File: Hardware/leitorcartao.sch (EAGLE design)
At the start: 166 parts, among them IC1 TL084, IC2 TL084, Q1 DMN3404, Q2 MMBT4401, Q3 MMBT4403, Q4 MMBT4401, Q5 MMBT4401, Q6 MMBT4401, Q7 MMBT4401, U1 LP2985-33DBVR, U2 TLV1117-50CDCYR, U3 SAMD20E14A-AUT, U4 MFRC52202HN1, X1 ANTENA, X2 MIFARE

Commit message: Novas alterações na BOM. Ainda sem os filtro de PSK e FSK.
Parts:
- BZ1, C1, C10, C11, C12, C13, C14, C15, C16, C17, C2, C3, C4, C5, C6, C63, C7, C8, C9, D1, D2, D4, D5, LED1, Q5, Q6, Q7, QZ1, R1, R2, R3, R48, R49, R50, R51, R52, R53, R54, R55, R56, R57, R58, R59, R60, R61, R62, R63, R64, U1, U2, U3: ASK (none) -> X; FSK (none) -> X; MIFARE (none) -> X; PSK (none) -> X
- C18, C19, C20, C23, C24, C26, R11, R12, R13, R14, R5, R7: ASK (none) -> X; SPECIAL ASK -> (none)
- C21, C22, C25, C27, C28, C30, C33, C34, D3, Q1, Q2, Q3, R10, R15, R16, R17, R20, R22, R24, R25, R4, R6, R8, R9: ASK (none) -> X; FSK (none) -> X; PSK (none) -> X
- C29, C35, C45: CUSTOMERPN C/0.1u/16V/A04 -> (none); FSK (none) -> X; PN1 CL05B104KO5NNNC -> (none); PSK (none) -> X; SPECIAL FSK/PSK -> (none)
- C31, C32, C38, C39, C43, C44, IC2, R21, R23, R27, R35, R36, R39, R40, R41: FSK (none) -> X; PSK (none) -> X; SPECIAL FSK/PSK -> (none)
- C36, C37, C40, C41, R29, R30, R32, R34, R37, R38: FSK (none) -> X; PSK (none) -> X
- C42, R33: ASK (none) -> X; FSK (none) -> X; PSK (none) -> X; SPECIAL FSK/PSK -> (none)
- C46, C47, C48, C49, C50, C51, C52, C53, C54, C55, C56, C57, C58, C59, C60, C61, L1, L2, L3, L4, QZ2, R42, R43, R44, R45, R46, R47: MIFARE (none) -> X; SPECIAL MIFARE -> (none)
- C62: SPECIAL MIFARE -> (none)
- C64: ASK (none) -> X; FSK (none) -> X; MIFARE (none) -> X; PSK (none) -> X; SPECIAL DNP -> (none)
- IC1: ASK (none) -> X; FSK (none) -> X; PSK (none) -> X; SPECIAL ASK -> (none)
- R18: ASK (none) -> X; CUSTOMERPN R/12k/5%/04 -> R/27k/1%/04; PN1 RC1608J123CS -> MCR01MRTF2702; SPECIAL ASK -> (none)
- R19: ASK (none) -> X; CUSTOMERPN R/5.1k/5%/04 -> R/9.1k/5%/04; PN1 ERJ-2GEJ512X -> RC1608J912CS; SPECIAL ASK -> (none)
- R26: CUSTOMERPN R/5.1k/5%/04 -> R/9.1k/5%/04; FSK (none) -> X; PN1 ERJ-2GEJ512X -> RC1608J912CS; PSK (none) -> X; SPECIAL FSK/PSK -> (none)
- R28: CUSTOMERPN R/12k/5%/04 -> R/27k/1%/04; FSK (none) -> X; PN1 RC1608J123CS -> MCR01MRTF2702; PSK (none) -> X; SPECIAL FSK/PSK -> (none)
- R31: FSK (none) -> X; PASSIVO (none) -> Sim; PSK (none) -> X; SPECIAL FSK/PSK -> (none)
- U4: MIFARE (none) -> X

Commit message: Finalização da BOM pelo Neto.
Alteração de customers PN errados.
Alteração de PN errados.
Seleção de componentes mais baratos.

Candidato para envio à AVNET.
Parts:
- C1, C4: PN1 EMK107ABJ475KA-T -> CL10A475KO8NNNC
- C12, C5, C8: PN1 CC0805ZKY5V6BB106 -> GRM188R61E106MA73D
- C13, C15: CUSTOMERPN C/0.1u/16V/A04 -> C/18p/50V/D06; PN1 CL05B104KO5NNNC -> CL05C180JB5NNNC
- C18, C26: CUSTOMERPN C/220n/200V/C12 -> C/220n/25V/C04; PN1 C3216X7R2A224K115AA -> C1005X5R1E224K050BC
- C27: PN1 C3216X7R2A224K115AA -> C3216X7T2E224K160AA
- C30: PN1 CC0402KRX7R9BB681 -> CL05B681KB5NNNC
- C46, C47: CUSTOMERPN C/18p/50V/D04 -> C/18p/50V/D06
- C51: PN1 (none) -> C0402C102J1GACTU
- C54, C55: PN1 CL05C121JB5NNNC -> 06035U121FAT2A
- C59, C60: PN1 CL05C560JB5NNNC -> 06031U560FAT2A
- D1, D3: PN1 BYG20J -> BYG20J-E3/TR
- D4, D5: CUSTOMERPN D/BAT54S -> D/BAT54S/SOT23
- L1, L2: PN1 (none) -> CIH05T22NJNC
- L3, L4: CUSTOMERPN L/1u/06/0.5A -> L/1u/0.5A/06; PN1 (none) -> BRC1608T1R0M
- Q4, Q5, Q6, Q7: PN1 MMBT4403LT3G -> MMBT4401LT3G
- R1, R2, R29: PN1 RC0402JR-07470RL -> 4-1622826-4
- R17: CUSTOMERPN R/100K/5%/06 -> R/1K/5%/04; PN1 RC0603JR-07100KL -> RC0402JR-071KL
- R18, R28, R30, R32, R34, R37: PN1 MCR01MRTF2702 -> RC1005F273CS
- R19, R20, R22, R26: PN1 RC1608J912CS -> RC1005J912CS
- R25: CUSTOMERPN R/12k/5%/04 -> R/13k/5%/04; PN1 RC1608J123CS -> RC1005J133CS
- R3: CUSTOMERPN R/10K/5%/04 -> R/12K/5%/04; PN1 RC0402JR-0710KL -> 1622826-8
- R38: CUSTOMERPN R/100/5%/04 -> R/100/5%/06
- R42, R43, R5, R7: PN1 RC0402JR-074K7L -> RC1608J472CS
- R45, R48, R49, R55, R6, R62: PN1 RC0402JR-072K2L -> RMCF0402JT2K20
- R46, R47: PN1 RC0402JR-073R3L -> RC1608J3R3CS
- R52, R57, R64: PN1 MCR01MRTF1000 -> RC1005J101CS

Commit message: Correção de erros na BOM.
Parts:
- C62: MIFARE (none) -> X
- Q4: ASK (none) -> X; FSK (none) -> X; MIFARE (none) -> X; PSK (none) -> X
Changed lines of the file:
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@@
 </part>
 <part name="Q4" library="RFiD" deviceset="MMBT4401" device="">
-<attribute name="ASK" value=""/>
+<attribute name="ASK" value="X"/>
 <attribute name="CUSTOMERPN" value="Q/MMBT4401/SOT23"/>
-<attribute name="FSK" value=""/>
-<attribute name="FSK_PN" value=""/>
-<attribute name="MIFARE" value=""/>
+<attribute name="FSK" value="X"/>
+<attribute name="FSK_PN" value=""/>
+<attribute name="MIFARE" value="X"/>
 <attribute name="PASSIVO" value=""/>
 <attribute name="PN1" value="MMBT4401LT3G"/>
-<attribute name="PSK" value=""/>
+<attribute name="PSK" value="X"/>
 <attribute name="PSK_PN" value=""/>
 <attribute name="SPECIAL" value=""/>
@@
 <attribute name="FSK" value=""/>
 <attribute name="FSK_PN" value=""/>
-<attribute name="MIFARE" value=""/>
+<attribute name="MIFARE" value="X"/>
 <attribute name="PASSIVO" value="Sim"/>
 <attribute name="PN1" value="CL05B104KO5NNNC"/>

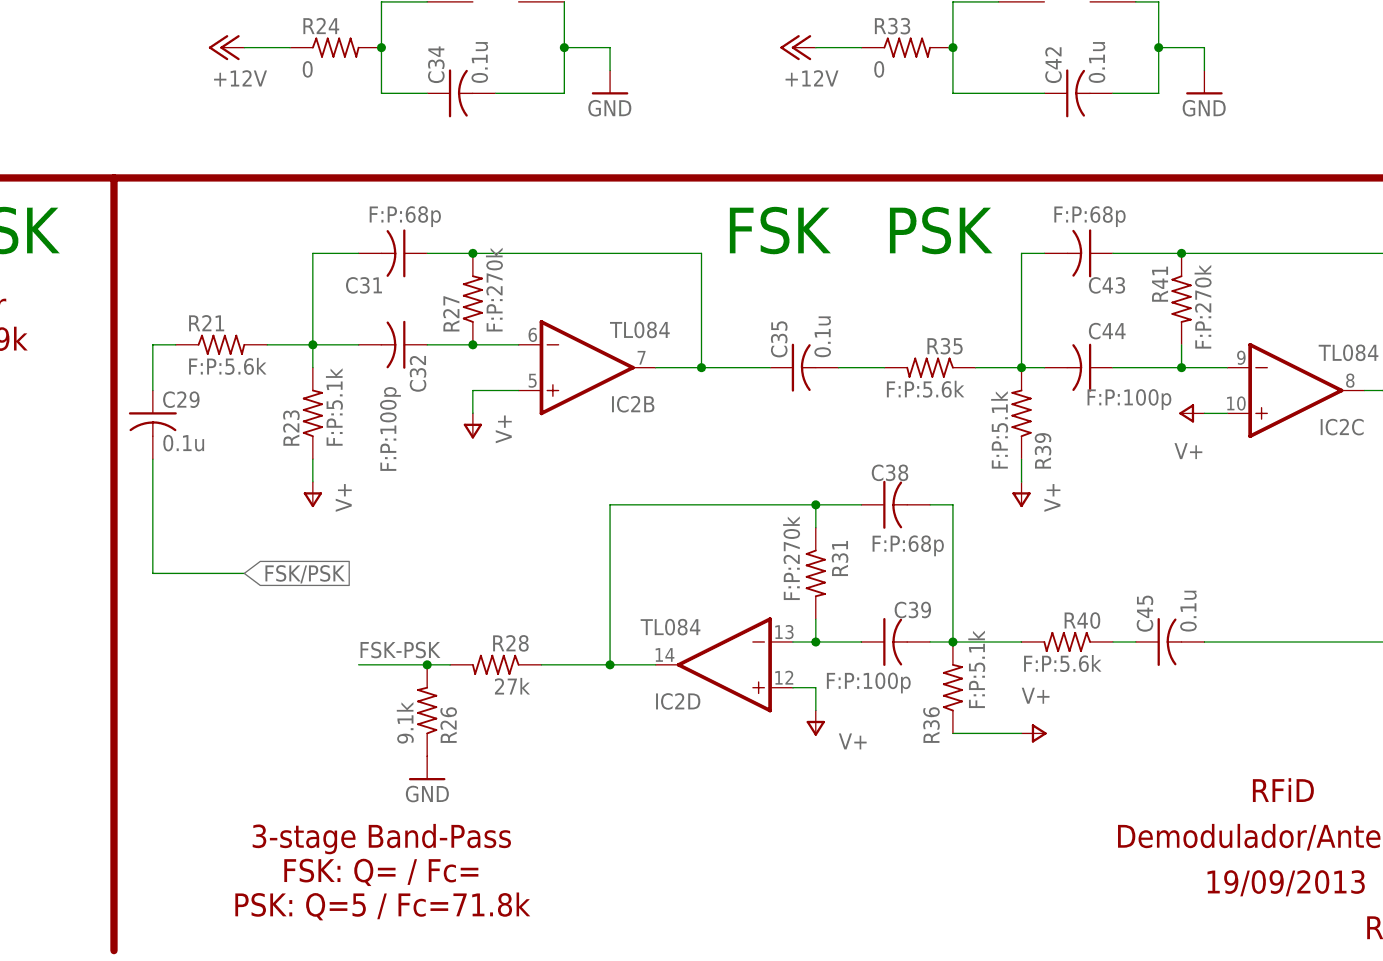
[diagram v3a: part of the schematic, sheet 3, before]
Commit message: Adição dos valores dos componentes dos filtros PSK/FSK.
Adição dos PN dos componentes dos filtros.
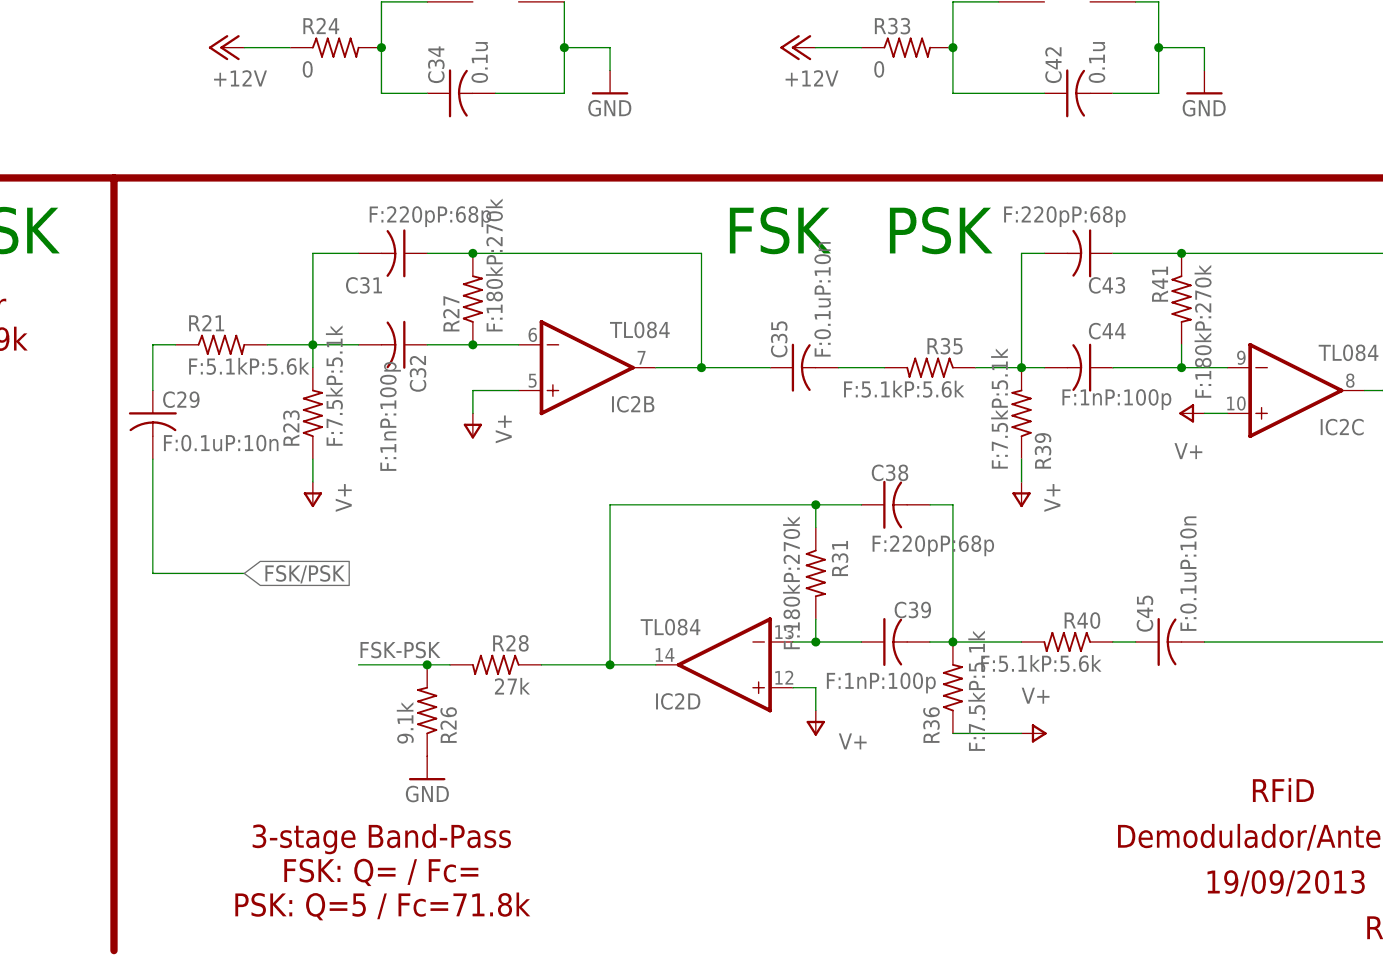
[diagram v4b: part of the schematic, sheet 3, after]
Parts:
- C29, C35, C45: value 0.1u -> F:0.1uP:10n; FSK_PN (none) -> CL05B104KO5NNNC; PSK_PN (none) -> CL05B103KB5NNNC
- C31, C38, C43: value F:P:68p -> F:220pP:68p; FSK_PN (none) -> CL05C221JB5NNNC; PSK_PN (none) -> CL05C680JB5NNNC
- C32, C39, C44: value F:P:100p -> F:1nP:100p; FSK_PN (none) -> C0402C102J1GACTU; PSK_PN (none) -> CL05C101JB5NNNC
- R21, R35, R40: value F:P:5.6k -> F:5.1kP:5.6k; FSK_PN (none) -> RC1005F512CS; PSK_PN (none) -> RC1005F562CS
- R23, R36, R39: value F:P:5.1k -> F:7.5kP:5.1k; FSK_PN (none) -> RC1005F752CS; PSK_PN (none) -> RC1005F512CS
- R27, R31, R41: value F:P:270k -> F:180kP:270k; FSK_PN (none) -> RC1005F184CS; PSK_PN (none) -> RC1005F274CS

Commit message: Novos campos adicionados na BOM para facilitar o pedido.
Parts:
- BZ1: ASK_CUSTOMERPN (none) -> BUZ-REP; ASK_PN (none) -> PS1240P02BT; CUSTOMERPN BUZ-REP -> (none); FSK_CUSTOMERPN (none) -> BUZ-REP; FSK_PN (none) -> PS1240P02BT; MIFARE_CUSTOMERPN (none) -> BUZ-REP; MIFARE_PN (none) -> PS1240P02BT; PN1 PS1240P02BT -> (none); PSK_CUSTOMERPN (none) -> BUZ-REP; PSK_PN (none) -> PS1240P02BT
- C1, C4: ASK_CUSTOMERPN (none) -> C/4.7u/16V/C06; ASK_PN (none) -> CL10A475KO8NNNC; CUSTOMERPN C/4.7u/16V/C06 -> (none); FSK_CUSTOMERPN (none) -> C/4.7u/16V/C06; FSK_PN (none) -> CL10A475KO8NNNC; MIFARE_CUSTOMERPN (none) -> C/4.7u/16V/C06; MIFARE_PN (none) -> CL10A475KO8NNNC; PN1 CL10A475KO8NNNC -> (none); PSK_CUSTOMERPN (none) -> C/4.7u/16V/C06; PSK_PN (none) -> CL10A475KO8NNNC
- C10, C11, C14, C16, C17, C6, C9: ASK_CUSTOMERPN (none) -> C/0.1u/16V/A04; ASK_PN (none) -> CL05B104KO5NNNC; CUSTOMERPN C/0.1u/16V/A04 -> (none); FSK_CUSTOMERPN (none) -> C/0.1u/16V/A04; FSK_PN (none) -> CL05B104KO5NNNC; MIFARE_CUSTOMERPN (none) -> C/0.1u/16V/A04; MIFARE_PN (none) -> CL05B104KO5NNNC; PN1 CL05B104KO5NNNC -> (none); PSK_CUSTOMERPN (none) -> C/0.1u/16V/A04; PSK_PN (none) -> CL05B104KO5NNNC
- C12, C5, C8: ASK_CUSTOMERPN (none) -> C/10u/25V/A08; ASK_PN (none) -> GRM188R61E106MA73D; CUSTOMERPN C/10u/25V/A08 -> (none); FSK_CUSTOMERPN (none) -> C/10u/25V/A08; FSK_PN (none) -> GRM188R61E106MA73D; MIFARE_CUSTOMERPN (none) -> C/10u/25V/A08; MIFARE_PN (none) -> GRM188R61E106MA73D; PN1 GRM188R61E106MA73D -> (none); PSK_CUSTOMERPN (none) -> C/10u/25V/A08; PSK_PN (none) -> GRM188R61E106MA73D
- C13, C15: ASK_CUSTOMERPN (none) -> C/18p/50V/D06; ASK_PN (none) -> CL05C180JB5NNNC; CUSTOMERPN C/18p/50V/D06 -> (none); FSK_CUSTOMERPN (none) -> C/18p/50V/D06; FSK_PN (none) -> CL05C180JB5NNNC; MIFARE_CUSTOMERPN (none) -> C/18p/50V/D06; MIFARE_PN (none) -> CL05C180JB5NNNC; PN1 CL05C180JB5NNNC -> (none); PSK_CUSTOMERPN (none) -> C/18p/50V/D06; PSK_PN (none) -> CL05C180JB5NNNC
- C18, C26: ASK_CUSTOMERPN (none) -> C/220n/25V/C04; ASK_PN (none) -> C1005X5R1E224K050BC; CUSTOMERPN C/220n/25V/C04 -> (none); PN1 C1005X5R1E224K050BC -> (none)
- C19, C20: ASK_CUSTOMERPN (none) -> C/4.7n/25V/D04; ASK_PN (none) -> CL05B472KA5NNNC; CUSTOMERPN C/4.7n/25V/D04 -> (none); PN1 CL05B472KA5NNNC -> (none)
- C2: ASK_CUSTOMERPN (none) -> C/1m/16V/PTH; ASK_PN (none) -> ESK108M016AH2AA; CUSTOMERPN C/1m/16V/PTH -> (none); FSK_CUSTOMERPN (none) -> C/1m/16V/PTH; FSK_PN (none) -> ESK108M016AH2AA; MIFARE_CUSTOMERPN (none) -> C/1m/16V/PTH; MIFARE_PN (none) -> ESK108M016AH2AA; PN1 ESK108M016AH2AA -> (none); PSK_CUSTOMERPN (none) -> C/1m/16V/PTH; PSK_PN (none) -> ESK108M016AH2AA
- C21: ASK_CUSTOMERPN (none) -> DNP; CUSTOMERPN DNP -> (none); FSK_CUSTOMERPN (none) -> DNP; FSK_PN (none) -> DNP; PSK_PN (none) -> DNP
- C22: ASK_CUSTOMERPN (none) -> C/1n/500V/E18; ASK_PN (none) -> C1812C102FBGACTU; CUSTOMERPN C/1n/500V/E18 -> (none); FSK_CUSTOMERPN (none) -> C/1n/500V/E18; FSK_PN (none) -> C1812C102FBGACTU; PN1 C1812C102FBGACTU -> (none); PSK_CUSTOMERPN (none) -> C/1n/500V/E18; PSK_PN (none) -> C1812C102FBGACTU
- C23, C24: ASK_CUSTOMERPN (none) -> C/68p/25V/D04; ASK_PN (none) -> CL05C680JB5NNNC; CUSTOMERPN C/68p/25V/D04 -> (none); PASSIVO Sim -> (none); PN1 CL05C680JB5NNNC -> (none)
- C25, C34, C42: ASK_CUSTOMERPN (none) -> C/0.1u/16V/A04; ASK_PN (none) -> CL05B104KO5NNNC; CUSTOMERPN C/0.1u/16V/A04 -> (none); FSK_CUSTOMERPN (none) -> C/0.1u/16V/A04; FSK_PN (none) -> CL05B104KO5NNNC; PN1 CL05B104KO5NNNC -> (none); PSK_CUSTOMERPN (none) -> C/0.1u/16V/A04; PSK_PN (none) -> CL05B104KO5NNNC
- C27: ASK_CUSTOMERPN (none) -> C/220n/200V/C12; ASK_PN (none) -> C3216X7T2E224K160AA; CUSTOMERPN C/220n/200V/C12 -> (none); FSK_CUSTOMERPN (none) -> C/220n/200V/C12; FSK_PN (none) -> C3216X7T2E224K160AA; PN1 C3216X7T2E224K160AA -> (none); PSK_CUSTOMERPN (none) -> C/220n/200V/C12; PSK_PN (none) -> C3216X7T2E224K160AA
- C28: ASK_CUSTOMERPN (none) -> C/1n/200V/C12; ASK_PN (none) -> CL31C102JHHNFNE; CUSTOMERPN C/1n/200V/C12 -> (none); FSK_CUSTOMERPN (none) -> C/1n/200V/C12; FSK_PN (none) -> CL31C102JHHNFNE; PN1 CL31C102JHHNFNE -> (none); PSK_CUSTOMERPN (none) -> C/1n/200V/C12; PSK_PN (none) -> CL31C102JHHNFNE
- C29: PSK_CUSTOMERPN (none) -> C/0.1u/16V/A04
- C3, C7: ASK_CUSTOMERPN (none) -> C/10n/50V/C04; ASK_PN (none) -> CL05B103KB5NNNC; CUSTOMERPN C/10n/50V/C04 -> (none); FSK_CUSTOMERPN (none) -> C/10n/50V/C04; FSK_PN (none) -> CL05B103KB5NNNC; MIFARE_CUSTOMERPN (none) -> C/10n/50V/C04; MIFARE_PN (none) -> CL05B103KB5NNNC; PN1 CL05B103KB5NNNC -> (none); PSK_CUSTOMERPN (none) -> C/10n/50V/C04; PSK_PN (none) -> CL05B103KB5NNNC
- C30: ASK_CUSTOMERPN (none) -> C/680p/25V/C04; ASK_PN (none) -> CL05B681KB5NNNC; CUSTOMERPN C/680p/25V/C04 -> (none); FSK_CUSTOMERPN (none) -> C/680p/25V/C04; FSK_PN (none) -> CL05B681KB5NNNC; PN1 CL05B681KB5NNNC -> (none); PSK_CUSTOMERPN (none) -> C/680p/25V/C04; PSK_PN (none) -> CL05B681KB5NNNC
- C31, C38: FSK_CUSTOMERPN (none) -> C/220p/25V/D04; PSK_CUSTOMERPN (none) -> C/68p/25V/D04
- C32, C39, C44: FSK_CUSTOMERPN (none) -> C/1n/100V/D04; PSK_CUSTOMERPN (none) -> C/100p/50V/D04
- C33: ASK_CUSTOMERPN (none) -> C/68p/25V/D04; ASK_PN (none) -> CL05C680JB5NNNC; CUSTOMERPN C/68p/25V/D04 -> (none); FSK_CUSTOMERPN (none) -> C/68p/25V/D04; FSK_PN (none) -> CL05C680JB5NNNC; PN1 CL05C680JB5NNNC -> (none); PSK_CUSTOMERPN (none) -> C/68p/25V/D04; PSK_PN (none) -> CL05C680JB5NNNC
- C35, C45: FSK_CUSTOMERPN (none) -> C/0.1u/16V/A04; PSK_CUSTOMERPN (none) -> C/10n/50V/C04
- C36, C37, C40, C41: CUSTOMERPN C/47p/25V/E04 -> (none); FSK_CUSTOMERPN (none) -> C/47p/25V/E04; FSK_PN (none) -> GRM1555C1H470FA01D; PN1 GRM1555C1H470FA01D -> (none); PSK_CUSTOMERPN (none) -> C/47p/25V/E04; PSK_PN (none) -> GRM1555C1H470FA01D
- C43: FSK_CUSTOMERPN (none) -> C/220p/25V/D04; PSK_CUSTOMERPN (none) -> C/680p/25V/C04
- C46, C47: CUSTOMERPN C/18p/50V/D06 -> (none); MIFARE_CUSTOMERPN (none) -> C/18p/50V/D06; MIFARE_PN (none) -> CL05C180JB5NNNC; PN1 CL05C180JB5NNNC -> (none)
- C48, C52, C53, C58, C61, C62: CUSTOMERPN C/0.1u/16V/A04 -> (none); MIFARE_CUSTOMERPN (none) -> C/0.1u/16V/A04; MIFARE_PN (none) -> CL05B104KO5NNNC; PN1 CL05B104KO5NNNC -> (none)
- C49, C50: CUSTOMERPN C/100p/50V/D04 -> (none); MIFARE_CUSTOMERPN (none) -> C/100p/50V/D04; MIFARE_PN (none) -> CL05C101JB5NNNC; PN1 CL05C101JB5NNNC -> (none)
- C51: CUSTOMERPN C/1n/100V/D04 -> (none); MIFARE_CUSTOMERPN (none) -> C/1n/100V/D04; MIFARE_PN (none) -> C0402C102J1GACTU; PN1 C0402C102J1GACTU -> (none)
- C54, C55: CUSTOMERPN C/120p/50V/E06 -> (none); MIFARE_CUSTOMERPN (none) -> C/120p/50V/E06; MIFARE_PN (none) -> 06035U121FAT2A; PN1 06035U121FAT2A -> (none)
- C56, C57: CUSTOMERPN C/18p/50V/E06 -> (none); MIFARE_CUSTOMERPN (none) -> C/18p/50V/E06; MIFARE_PN (none) -> CL05C180JB5NNNC; PN1 CL05C180JB5NNNC -> (none)
- C59, C60: CUSTOMERPN C/56p/100V/E06 -> (none); MIFARE_CUSTOMERPN (none) -> C/56p/100V/E06; MIFARE_PN (none) -> 06031U560FAT2A; PN1 06031U560FAT2A -> (none)
- C63: ASK_CUSTOMERPN (none) -> C/0.1u/16V/A04; ASK_PN (none) -> CL05B104KO5NNNC; CUSTOMERPN C/0.1u/16V/A04 -> (none); FSK_CUSTOMERPN (none) -> C/0.1u/16V/A04; FSK_PN (none) -> CL05B104KO5NNNC; MIFARE_CUSTOMERPN (none) -> C/0.1u/16V/A04; MIFARE_PN (none) -> CL05B104KO5NNNC; PN1 CL05B104KO5NNNC -> (none); PSK_CUSTOMERPN (none) -> CL05B104KO5NNNC; PSK_PN (none) -> C/0.1u/16V/A04
- C64: ASK_CUSTOMERPN (none) -> DNP; ASK_PN (none) -> CL05B104KO5NNNC; CUSTOMERPN DNP -> (none); FSK_CUSTOMERPN (none) -> DNP; FSK_PN (none) -> CL05B104KO5NNNC; MIFARE_CUSTOMERPN (none) -> DNP; MIFARE_PN (none) -> CL05B104KO5NNNC; PN1 CL05B104KO5NNNC -> (none); PSK_CUSTOMERPN (none) -> CL05B104KO5NNNC; PSK_PN (none) -> DNP
- CARDPRS, D0/TX/CLK, D1/DATA, GND, LED-IN, MODE, SWD, VCC, X1, X2: CUSTOMERPN DNP -> (none)
- D1: ASK_CUSTOMERPN (none) -> D/BYG20J; ASK_PN (none) -> BYG20J-E3/TR; CUSTOMERPN D/BYG20J -> (none); FSK_CUSTOMERPN (none) -> D/BYG20J; FSK_PN (none) -> BYG20J-E3/TR; MIFARE_CUSTOMERPN (none) -> D/BYG20J; MIFARE_PN (none) -> BYG20J-E3/TR; PN1 BYG20J-E3/TR -> (none); PSK_CUSTOMERPN (none) -> D/BYG20J; PSK_PN (none) -> BYG20J-E3/TR
- D2: ASK_CUSTOMERPN (none) -> TVS/14V/SMA; ASK_PN (none) -> SMAJ14A; CUSTOMERPN TVS/14V/SMA -> (none); FSK_CUSTOMERPN (none) -> TVS/14V/SMA; FSK_PN (none) -> SMAJ14A; MIFARE_CUSTOMERPN (none) -> TVS/14V/SMA; MIFARE_PN (none) -> SMAJ14A; PN1 SMAJ14A -> (none); PSK_CUSTOMERPN (none) -> TVS/14V/SMA; PSK_PN (none) -> SMAJ14A
- D3: ASK_CUSTOMERPN (none) -> D/BYG20J; ASK_PN (none) -> BYG20J-E3/TR; CUSTOMERPN D/BYG20J -> (none); FSK_CUSTOMERPN (none) -> D/BYG20J; FSK_PN (none) -> BYG20J-E3/TR; PN1 BYG20J-E3/TR -> (none); PSK_CUSTOMERPN (none) -> D/BYG20J; PSK_PN (none) -> BYG20J-E3/TR
- D4, D5: ASK_CUSTOMERPN (none) -> D/BAT54S/SOT23; ASK_PN (none) -> BAT54S,215; CUSTOMERPN D/BAT54S/SOT23 -> (none); FSK_CUSTOMERPN (none) -> D/BAT54S/SOT23; FSK_PN (none) -> BAT54S,215; MIFARE_CUSTOMERPN (none) -> D/BAT54S/SOT23; MIFARE_PN (none) -> BAT54S,215; PN1 BAT54S,215 -> (none); PSK_CUSTOMERPN (none) -> D/BAT54S/SOT23; PSK_PN (none) -> BAT54S,215
- IC1: ASK_CUSTOMERPN (none) -> IC/TL084/TSSOP14; ASK_PN (none) -> TL084CPT; CUSTOMERPN IC/TL084/TSSOP14 -> (none); FSK_CUSTOMERPN (none) -> IC/TL084/TSSOP14; FSK_PN (none) -> TL084CPT; PN1 TL084CPT -> (none); PSK_CUSTOMERPN (none) -> IC/TL084/TSSOP14; PSK_PN (none) -> TL084CPT
- IC2: CUSTOMERPN IC/TL084/TSSOP14 -> (none); FSK_CUSTOMERPN (none) -> IC/TL084/TSSOP14; FSK_PN (none) -> TL084CPT; PN1 TL084CPT -> (none); PSK_CUSTOMERPN (none) -> IC/TL084/TSSOP14; PSK_PN (none) -> TL084CPT
- L1, L2: CUSTOMERPN L/22n/0.2A/04 -> (none); MIFARE_CUSTOMERPN (none) -> L/22n/0.2A/04; MIFARE_PN (none) -> CIH05T22NJNC; PN1 CIH05T22NJNC -> (none)
- L3, L4: CUSTOMERPN L/1u/0.5A/06 -> (none); MIFARE_CUSTOMERPN (none) -> L/1u/0.5A/06; MIFARE_PN (none) -> BRC1608T1R0M; PN1 BRC1608T1R0M -> (none)
- LED1: ASK_CUSTOMERPN (none) -> LED/RG/3MM; ASK_PN (none) -> LTL1BEKVJNN; CUSTOMERPN LED/RG/3MM -> (none); FSK_CUSTOMERPN (none) -> LED/RG/3MM; FSK_PN (none) -> LTL1BEKVJNN; MIFARE_CUSTOMERPN (none) -> LED/RG/3MM; MIFARE_PN (none) -> LTL1BEKVJNN; PN1 LTL1BEKVJNN -> (none); PSK_CUSTOMERPN (none) -> LED/RG/3MM; PSK_PN (none) -> LTL1BEKVJNN
- Q1: ASK_CUSTOMERPN (none) -> Q/DMN3404/SOT23; ASK_PN (none) -> DMN3404L-7; CUSTOMERPN Q/DMN3404/SOT23 -> (none); FSK_CUSTOMERPN (none) -> Q/DMN3404/SOT23; FSK_PN (none) -> DMN3404L-7; PN1 DMN3404L-7 -> (none); PSK_CUSTOMERPN (none) -> Q/DMN3404/SOT23; PSK_PN (none) -> DMN3404L-7
- Q2: ASK_CUSTOMERPN (none) -> Q/MMBT4401/SOT23; ASK_PN (none) -> MMBT4401LT3G; CUSTOMERPN Q/MMBT4401/SOT23 -> (none); FSK_CUSTOMERPN (none) -> Q/MMBT4401/SOT23; FSK_PN (none) -> MMBT4401LT3G; PN1 MMBT4401LT3G -> (none); PSK_CUSTOMERPN (none) -> Q/MMBT4401/SOT23; PSK_PN (none) -> MMBT4401LT3G
- Q3: ASK_CUSTOMERPN (none) -> Q/MMBT4403/SOT23; ASK_PN (none) -> MMBT4403LT3G; CUSTOMERPN Q/MMBT4403/SOT23 -> (none); FSK_CUSTOMERPN (none) -> Q/MMBT4403/SOT23; FSK_PN (none) -> MMBT4403LT3G; PN1 MMBT4403LT3G -> (none); PSK_CUSTOMERPN (none) -> Q/MMBT4403/SOT23; PSK_PN (none) -> MMBT4403LT3G
- Q4, Q5, Q6, Q7: ASK_CUSTOMERPN (none) -> Q/MMBT4401/SOT23; ASK_PN (none) -> MMBT4401LT3G; CUSTOMERPN Q/MMBT4401/SOT23 -> (none); FSK_CUSTOMERPN (none) -> Q/MMBT4401/SOT23; FSK_PN (none) -> MMBT4401LT3G; MIFARE_CUSTOMERPN (none) -> Q/MMBT4401/SOT23; MIFARE_PN (none) -> MMBT4401LT3G; PN1 MMBT4401LT3G -> (none); PSK_CUSTOMERPN (none) -> Q/MMBT4401/SOT23; PSK_PN (none) -> MMBT4401LT3G
- QZ1: ASK_CUSTOMERPN (none) -> XTAL/8MHZ/PTH; ASK_PN (none) -> 9B-8.000MAAJ-B; CUSTOMERPN XTAL/8MHZ/PTH -> (none); FSK_CUSTOMERPN (none) -> XTAL/8MHZ/PTH; FSK_PN (none) -> 9B-8.000MAAJ-B; MIFARE_CUSTOMERPN (none) -> XTAL/8MHZ/PTH; MIFARE_PN (none) -> 9B-8.000MAAJ-B; PN1 9B-8.000MAAJ-B -> (none); PSK_CUSTOMERPN (none) -> XTAL/8MHZ/PTH; PSK_PN (none) -> 9B-8.000MAAJ-B
- QZ2: CUSTOMERPN XTAL/2712MHZ/5x3 -> (none); MIFARE_CUSTOMERPN (none) -> XTAL/2712MHZ/5x3; MIFARE_PN (none) -> 7B-27.120MAAJ-T; PN1 7B-27.120MAAJ-T -> (none)
- R1, R2: ASK_CUSTOMERPN (none) -> R/470/5%/04; ASK_PN (none) -> 4-1622826-4; CUSTOMERPN R/470/5%/04 -> (none); FSK_CUSTOMERPN (none) -> R/470/5%/04; FSK_PN (none) -> 4-1622826-4; MIFARE_CUSTOMERPN (none) -> R/470/5%/04; MIFARE_PN (none) -> 4-1622826-4; PN1 4-1622826-4 -> (none); PSK_CUSTOMERPN (none) -> R/470/5%/04; PSK_PN (none) -> 4-1622826-4
- R10, R9: ASK_CUSTOMERPN (none) -> R/10/5%/06; ASK_PN (none) -> RC1608J100CS; CUSTOMERPN R/10/5%/06 -> (none); FSK_CUSTOMERPN (none) -> R/10/5%/06; FSK_PN (none) -> RC1608J100CS; PN1 RC1608J100CS -> (none); PSK_CUSTOMERPN (none) -> R/10/5%/06; PSK_PN (none) -> RC1608J100CS
- R11: ASK_CUSTOMERPN (none) -> R/91k/5%/04; ASK_PN (none) -> RMCF0402JT91K0; CUSTOMERPN R/91k/5%/04 -> (none); FSK_PN (none) -> RMCF0402JT91K0; PN1 RMCF0402JT91K0 -> (none)
- R12, R14: ASK_CUSTOMERPN (none) -> R/13k/5%/04; ASK_PN (none) -> RC1005J133CS; CUSTOMERPN R/13k/5%/04 -> (none); PN1 RC1005J133CS -> (none)
- R13: ASK_CUSTOMERPN (none) -> R/91k/5%/04; ASK_PN (none) -> RMCF0402JT91K0; CUSTOMERPN R/91k/5%/04 -> (none); PN1 RMCF0402JT91K0 -> (none)
- R15: ASK_CUSTOMERPN (none) -> R/1M/5%/12; ASK_PN (none) -> RC3216J105CS; CUSTOMERPN R/1M/5%/12 -> (none); FSK_CUSTOMERPN (none) -> R/1M/5%/12; FSK_PN (none) -> RC3216J105CS; PN1 RC3216J105CS -> (none); PSK_CUSTOMERPN (none) -> R/1M/5%/12; PSK_PN (none) -> RC3216J105CS
- R16: ASK_CUSTOMERPN (none) -> R/100K/5%/06; ASK_PN (none) -> RC0603JR-07100KL; CUSTOMERPN R/100K/5%/06 -> (none); FSK_CUSTOMERPN (none) -> R/100K/5%/06; FSK_PN (none) -> RC0603JR-07100KL; PN1 RC0603JR-07100KL -> (none); PSK_CUSTOMERPN (none) -> R/100K/5%/06; PSK_PN (none) -> RC0603JR-07100KL
- R17, R4: ASK_CUSTOMERPN (none) -> R/1K/5%/04; ASK_PN (none) -> RC0402JR-071KL; CUSTOMERPN R/1K/5%/04 -> (none); FSK_CUSTOMERPN (none) -> R/1K/5%/04; FSK_PN (none) -> RC0402JR-071KL; PN1 RC0402JR-071KL -> (none); PSK_CUSTOMERPN (none) -> R/1K/5%/04; PSK_PN (none) -> RC0402JR-071KL
- R18: ASK_CUSTOMERPN (none) -> R/27k/1%/04; ASK_PN (none) -> RC1005F273CS; CUSTOMERPN R/27k/1%/04 -> (none); PN1 RC1005F273CS -> (none)
- R19: ASK_CUSTOMERPN (none) -> R/9.1k/5%/04; ASK_PN (none) -> RC1005J912CS; CUSTOMERPN R/9.1k/5%/04 -> (none); PN1 RC1005J912CS -> (none)
- R20: ASK_CUSTOMERPN (none) -> R/9.1k/5%/04; ASK_PN (none) -> RC1005J912CS; CUSTOMERPN R/9.1k/5%/04 -> (none); FSK_CUSTOMERPN (none) -> R/9.1k/5%/04; FSK_PN (none) -> CL05B104KO5NNNC; PN1 RC1005J912CS -> (none); PSK_CUSTOMERPN (none) -> R/9.1k/5%/04; PSK_PN (none) -> CL05B104KO5NNNC
- R21, R35, R40: FSK_CUSTOMERPN (none) -> R/5.1k/5%/04; PSK_CUSTOMERPN (none) -> R/5.6k/5%/04
- R22: ASK_CUSTOMERPN (none) -> R/9.1k/5%/04; ASK_PN (none) -> RC1005J912CS; CUSTOMERPN R/9.1k/5%/04 -> (none); FSK_CUSTOMERPN (none) -> R/9.1k/5%/04; FSK_PN (none) -> RC1005J912CS; PN1 RC1005J912CS -> (none); PSK_CUSTOMERPN (none) -> RC1005J912CS; PSK_PN (none) -> R/9.1k/5%/04
- R23, R36, R39: FSK_CUSTOMERPN (none) -> R/7.5k/5%/04; PSK_CUSTOMERPN (none) -> R/5.1k/5%/04
- R24, R33, R8: ASK_CUSTOMERPN (none) -> R/0/0%/04; ASK_PN (none) -> RC1005J000CS; CUSTOMERPN R/0/0%/04 -> (none); FSK_CUSTOMERPN (none) -> R/0/0%/04; FSK_PN (none) -> RC1005J000CS; PN1 RC1005J000CS -> (none); PSK_CUSTOMERPN (none) -> R/0/0%/04; PSK_PN (none) -> RC1005J000CS
- R25: ASK_CUSTOMERPN (none) -> R/13k/5%/04; ASK_PN (none) -> RC1005J133CS; CUSTOMERPN R/13k/5%/04 -> (none); FSK_CUSTOMERPN (none) -> R/13k/5%/04; FSK_PN (none) -> RC1005J133CS; PN1 RC1005J133CS -> (none); PSK_CUSTOMERPN (none) -> R/13k/5%/04; PSK_PN (none) -> RC1005J133CS
- R26: CUSTOMERPN R/9.1k/5%/04 -> (none); FSK_CUSTOMERPN (none) -> R/9.1k/5%/04; FSK_PN (none) -> RC1005J912CS; PN1 RC1005J912CS -> (none); PSK_CUSTOMERPN (none) -> R/9.1k/5%/04; PSK_PN (none) -> RC1005J912CS
- R27, R31, R41: FSK_CUSTOMERPN (none) -> R/180k/5%/04; FSK_PN RC1005F184CS -> 1-1622826-4; PSK_CUSTOMERPN (none) -> R/270k/5%/04
- R28, R30, R32, R34, R37: CUSTOMERPN R/27k/1%/04 -> (none); FSK_CUSTOMERPN (none) -> R/27k/1%/04; FSK_PN (none) -> RC1005F273CS; PN1 RC1005F273CS -> (none); PSK_CUSTOMERPN (none) -> R/27k/1%/04; PSK_PN (none) -> RC1005F273CS
- R29: CUSTOMERPN R/470/5%/04 -> (none); FSK_CUSTOMERPN (none) -> R/470/5%/04; FSK_PN (none) -> 4-1622826-4; PN1 4-1622826-4 -> (none); PSK_CUSTOMERPN (none) -> R/470/5%/04; PSK_PN (none) -> 4-1622826-4
- R3: ASK_CUSTOMERPN (none) -> R/12K/5%/04; ASK_PN (none) -> 1622826-8; CUSTOMERPN R/12K/5%/04 -> (none); FSK_CUSTOMERPN (none) -> R/12K/5%/04; FSK_PN (none) -> 1622826-8; MIFARE_CUSTOMERPN (none) -> R/12K/5%/04; MIFARE_PN (none) -> 1622826-8; PN1 1622826-8 -> (none); PSK_CUSTOMERPN (none) -> R/12K/5%/04; PSK_PN (none) -> 1622826-8
- R38: CUSTOMERPN R/100/5%/06 -> (none); FSK_CUSTOMERPN (none) -> R/100/5%/06; FSK_PN (none) -> RC1005J101CS; PN1 RC1005J101CS -> (none); PSK_CUSTOMERPN (none) -> R/100/5%/06; PSK_PN (none) -> RC1005J101CS
- R42, R43: CUSTOMERPN R/4.7K/5%/04 -> (none); MIFARE_CUSTOMERPN (none) -> R/4.7K/5%/04; MIFARE_PN (none) -> RC1608J472CS; PN1 RC1608J472CS -> (none)
- R44: CUSTOMERPN R/1K/5%/04 -> (none); MIFARE_CUSTOMERPN (none) -> R/1K/5%/04; MIFARE_PN (none) -> RC0402JR-071KL; PN1 RC0402JR-071KL -> (none)
- R45: CUSTOMERPN R/2.2k/5%/04 -> (none); MIFARE_CUSTOMERPN (none) -> R/2.2k/5%/04; MIFARE_PN (none) -> RMCF0402JT2K20; PN1 RMCF0402JT2K20 -> (none)
- R46, R47: CUSTOMERPN R/3.3/5%/06 -> (none); MIFARE_CUSTOMERPN (none) -> R/3.3/5%/06; MIFARE_PN (none) -> RC1608J3R3CS; PN1 RC1608J3R3CS -> (none)
- R48, R49, R55, R62: ASK_CUSTOMERPN (none) -> R/2.2k/5%/04; ASK_PN (none) -> RMCF0402JT2K20; CUSTOMERPN R/2.2k/5%/04 -> (none); FSK_CUSTOMERPN (none) -> R/2.2k/5%/04; FSK_PN (none) -> RMCF0402JT2K20; MIFARE_CUSTOMERPN (none) -> R/2.2k/5%/04; MIFARE_PN (none) -> RMCF0402JT2K20; PN1 RMCF0402JT2K20 -> (none); PSK_CUSTOMERPN (none) -> R/2.2k/5%/04; PSK_PN (none) -> RMCF0402JT2K20
- R5, R7: ASK_CUSTOMERPN (none) -> R/4.7k/5%/04; ASK_PN (none) -> RC1608J472CS; CUSTOMERPN R/4.7k/5%/04 -> (none); PN1 RC1608J472CS -> (none)
- R50, R51, R56, R63: ASK_CUSTOMERPN (none) -> R/1K/5%/04; ASK_PN (none) -> RC0402JR-071KL; CUSTOMERPN R/1K/5%/04 -> (none); FSK_CUSTOMERPN (none) -> R/1K/5%/04; FSK_PN (none) -> RC0402JR-071KL; MIFARE_CUSTOMERPN (none) -> R/1K/5%/04; MIFARE_PN (none) -> RC0402JR-071KL; PN1 RC0402JR-071KL -> (none); PSK_CUSTOMERPN (none) -> R/1K/5%/04; PSK_PN (none) -> RC0402JR-071KL
- R52, R57, R64: ASK_CUSTOMERPN (none) -> R/100/5%/06; ASK_PN (none) -> RC1005J101CS; CUSTOMERPN R/100/5%/06 -> (none); FSK_CUSTOMERPN (none) -> R/100/5%/06; FSK_PN (none) -> RC1005J101CS; MIFARE_CUSTOMERPN (none) -> R/100/5%/06; MIFARE_PN (none) -> RC1005J101CS; PN1 RC1005J101CS -> (none); PSK_CUSTOMERPN (none) -> R/100/5%/06; PSK_PN (none) -> RC1005J101CS
- R53: ASK_CUSTOMERPN (none) -> R/130/5%/04; ASK_PN (none) -> RC1005J131CS; CUSTOMERPN R/130/5%/04 -> (none); FSK_CUSTOMERPN (none) -> R/130/5%/04; FSK_PN (none) -> RC1005J131CS; MIFARE_CUSTOMERPN (none) -> R/130/5%/04; MIFARE_PN (none) -> RC1005J131CS; PN1 RC1005J131CS -> (none); PSK_CUSTOMERPN (none) -> R/130/5%/04; PSK_PN (none) -> RC1005J131CS
- R54: ASK_CUSTOMERPN (none) -> R/120/5%/04; ASK_PN (none) -> RC1005J121CS; CUSTOMERPN R/120/5%/04 -> (none); FSK_CUSTOMERPN (none) -> R/120/5%/04; FSK_PN (none) -> RC1005J121CS; MIFARE_CUSTOMERPN (none) -> R/120/5%/04; MIFARE_PN (none) -> RC1005J121CS; PN1 RC1005J121CS -> (none); PSK_CUSTOMERPN (none) -> R/120/5%/04; PSK_PN (none) -> RC1005J121CS
- R58, R59, R60, R61: ASK_CUSTOMERPN (none) -> R/100K/5%/06; ASK_PN (none) -> RC0603JR-07100KL; CUSTOMERPN R/100K/5%/06 -> (none); FSK_CUSTOMERPN (none) -> R/100K/5%/06; FSK_PN (none) -> RC0603JR-07100KL; MIFARE_CUSTOMERPN (none) -> R/100K/5%/06; MIFARE_PN (none) -> RC0603JR-07100KL; PN1 RC0603JR-07100KL -> (none); PSK_CUSTOMERPN (none) -> R/100K/5%/06; PSK_PN (none) -> RC0603JR-07100KL
- R6: ASK_CUSTOMERPN (none) -> R/2.2k/5%/04; ASK_PN (none) -> RMCF0402JT2K20; CUSTOMERPN R/2.2k/5%/04 -> (none); FSK_CUSTOMERPN (none) -> R/2.2k/5%/04; FSK_PN (none) -> RMCF0402JT2K20; PN1 RMCF0402JT2K20 -> (none); PSK_CUSTOMERPN (none) -> RMCF0402JT2K20; PSK_PN (none) -> R/2.2k/5%/04
- U1: ASK_CUSTOMERPN (none) -> IC/3V3REG; ASK_PN (none) -> LP2985-33DBVR; CUSTOMERPN IC/3V3REG -> (none); FSK_CUSTOMERPN (none) -> IC/3V3REG; FSK_PN (none) -> LP2985-33DBVR; MIFARE_CUSTOMERPN (none) -> IC/3V3REG; MIFARE_PN (none) -> LP2985-33DBVR; PN1 LP2985-33DBVR -> (none); PSK_CUSTOMERPN (none) -> IC/3V3REG; PSK_PN (none) -> LP2985-33DBVR
- U2: ASK_CUSTOMERPN (none) -> IC/5VREG; ASK_PN (none) -> TLV1117-50CDCYR; CUSTOMERPN IC/5VREG -> (none); FSK_CUSTOMERPN (none) -> IC/5VREG; FSK_PN (none) -> TLV1117-50CDCYR; MIFARE_CUSTOMERPN (none) -> IC/5VREG; MIFARE_PN (none) -> TLV1117-50CDCYR; PN1 TLV1117-50CDCYR -> (none); PSK_CUSTOMERPN (none) -> IC/5VREG; PSK_PN (none) -> TLV1117-50CDCYR
- U3: ASK_CUSTOMERPN (none) -> IC/SAMD20/TQ32; ASK_PN (none) -> SAMD20E14A-AUT; CUSTOMERPN IC/SAMD20/TQ32 -> (none); FSK_CUSTOMERPN (none) -> IC/SAMD20/TQ32; FSK_PN (none) -> SAMD20E14A-AUT; MIFARE_CUSTOMERPN (none) -> IC/SAMD20/TQ32; MIFARE_PN (none) -> SAMD20E14A-AUT; PN1 SAMD20E14A-AUT -> (none); PSK_CUSTOMERPN (none) -> IC/SAMD20/TQ32; PSK_PN (none) -> SAMD20E14A-AUT
- U4: CUSTOMERPN IC/MFRC52202 -> (none); MIFARE_CUSTOMERPN (none) -> IC/MFRC52202; MIFARE_PN (none) -> MFRC52202HN1,151; PN1 MFRC52202HN1,151 -> (none)

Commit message: Novas alterações na BOM com correção de campos errados.
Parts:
- C29: FSK_CUSTOMERPN (none) -> C/0.1u/16V/A04; PSK_CUSTOMERPN C/0.1u/16V/A04 -> C/10n/50V/C04
- C43: PSK_PN CL05C680JB5NNNC -> CL05B681KB5NNNC
- C63: PSK_CUSTOMERPN CL05B104KO5NNNC -> C/0.1u/16V/A04; PSK_PN C/0.1u/16V/A04 -> CL05B104KO5NNNC
- C64: PSK_CUSTOMERPN CL05B104KO5NNNC -> DNP; PSK_PN DNP -> CL05B104KO5NNNC
- R20: FSK_PN CL05B104KO5NNNC -> RC1005J912CS; PSK_PN CL05B104KO5NNNC -> RC1005J912CS
- R22: PSK_CUSTOMERPN RC1005J912CS -> R/9.1k/5%/04; PSK_PN R/9.1k/5%/04 -> RC1005J912CS
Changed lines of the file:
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@@
 <attribute name="CUSTOMERPN" value=""/>
 <attribute name="FSK" value="X"/>
-<attribute name="FSK_CUSTOMERPN" value=""/>
+<attribute name="FSK_CUSTOMERPN" value="C/0.1u/16V/A04"/>
 <attribute name="FSK_PN" value="CL05B104KO5NNNC"/>
 <attribute name="MIFARE" value=""/>
@@
 <attribute name="PN1" value=""/>
 <attribute name="PSK" value="X"/>
-<attribute name="PSK_CUSTOMERPN" value="C/0.1u/16V/A04"/>
+<attribute name="PSK_CUSTOMERPN" value="C/10n/50V/C04"/>
 <attribute name="PSK_PN" value="CL05B103KB5NNNC"/>
 <attribute name="SPECIAL" value=""/>
@@
 <attribute name="PSK" value="X"/>
 <attribute name="PSK_CUSTOMERPN" value="C/680p/25V/C04"/>
-<attribute name="PSK_PN" value="CL05C680JB5NNNC"/>
+<attribute name="PSK_PN" value="CL05B681KB5NNNC"/>
 <attribute name="SPECIAL" value=""/>
 </part>
@@
 <attribute name="FSK" value="X"/>
 <attribute name="FSK_CUSTOMERPN" value="R/9.1k/5%/04"/>
-<attribute name="FSK_PN" value="CL05B104KO5NNNC"/>
+<attribute name="FSK_PN" value="RC1005J912CS"/>
 <attribute name="MIFARE" value=""/>
 <attribute name="MIFARE_CUSTOMERPN" value=""/>
@@
 <attribute name="PSK" value="X"/>
 <attribute name="PSK_CUSTOMERPN" value="R/9.1k/5%/04"/>
-<attribute name="PSK_PN" value="CL05B104KO5NNNC"/>
+<attribute name="PSK_PN" value="RC1005J912CS"/>
 <attribute name="SPECIAL" value=""/>
 </part>
@@
 <attribute name="PN1" value=""/>
 <attribute name="PSK" value="X"/>
-<attribute name="PSK_CUSTOMERPN" value="RC1005J912CS"/>
-<attribute name="PSK_PN" value="R/9.1k/5%/04"/>
+<attribute name="PSK_CUSTOMERPN" value="R/9.1k/5%/04"/>
+<attribute name="PSK_PN" value="RC1005J912CS"/>
 <attribute name="SPECIAL" value=""/>
 </part>
@@
 <attribute name="PN1" value=""/>
 <attribute name="PSK" value="X"/>
-<attribute name="PSK_CUSTOMERPN" value="CL05B104KO5NNNC"/>
-<attribute name="PSK_PN" value="C/0.1u/16V/A04"/>
+<attribute name="PSK_CUSTOMERPN" value="C/0.1u/16V/A04"/>
+<attribute name="PSK_PN" value="CL05B104KO5NNNC"/>
 <attribute name="SPECIAL" value=""/>
 </part>
@@
 <attribute name="PN1" value=""/>
 <attribute name="PSK" value="X"/>
-<attribute name="PSK_CUSTOMERPN" value="CL05B104KO5NNNC"/>
-<attribute name="PSK_PN" value="DNP"/>
-<attribute name="SPECIAL" value=""/>
-</part>
+<attribute name="PSK_CUSTOMERPN" value="DNP"/>
+<attribute name="PSK_PN" value="CL05B104KO5NNNC"/>
+<attribute name="SPECIAL" value=""/>
+</part>

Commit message: Alteração de PN para componentes Samsung.
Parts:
- C13, C15: ASK_CUSTOMERPN C/18p/50V/D06 -> C/18p/100V/E06; ASK_PN CL05C180JB5NNNC -> 06031U180FAT2A; FSK_CUSTOMERPN C/18p/50V/D06 -> C/18p/100V/E06; FSK_PN CL05C180JB5NNNC -> 06031U180FAT2A; MIFARE_CUSTOMERPN C/18p/50V/D06 -> C/18p/100V/E06; MIFARE_PN CL05C180JB5NNNC -> 06031U180FAT2A; PSK_CUSTOMERPN C/18p/50V/D06 -> C/18p/100V/E06; PSK_PN CL05C180JB5NNNC -> 06031U180FAT2A
- C21: FSK_PN DNP -> (none)
- C36, C37, C40, C41: FSK_PN GRM1555C1H470FA01D -> CL05C470FB5NNNC; PSK_PN GRM1555C1H470FA01D -> CL05C470FB5NNNC
- C46, C47: MIFARE_CUSTOMERPN C/18p/50V/D06 -> C/18p/100V/E06; MIFARE_PN CL05C180JB5NNNC -> 06031U180FAT2A
- C54, C55: MIFARE_CUSTOMERPN C/120p/50V/E06 -> C/120p/100V/E06; MIFARE_PN 06035U121FAT2A -> GRM1885C2A121FA01J
- C56, C57: MIFARE_CUSTOMERPN C/18p/50V/E06 -> C/18p/100V/E06; MIFARE_PN CL05C180JB5NNNC -> 06031U180FAT2A
- R1, R2: ASK_PN 4-1622826-4 -> RC1005J471CS; FSK_PN 4-1622826-4 -> RC1005J471CS; MIFARE_PN 4-1622826-4 -> RC1005J471CS; PSK_PN 4-1622826-4 -> RC1005J471CS
- R11: ASK_PN RMCF0402JT91K0 -> RC1005J913CS; FSK_PN RMCF0402JT91K0 -> (none)
- R13: ASK_PN RMCF0402JT91K0 -> RC1005J913CS
- R27, R31, R41: FSK_PN 1-1622826-4 -> RC1005J184CS
- R29: FSK_PN 4-1622826-4 -> RC1005J471CS; PSK_PN 4-1622826-4 -> RC1005J471CS
- R3: ASK_PN 1622826-8 -> RC1005J123CS; FSK_PN 1622826-8 -> RC1005J123CS; MIFARE_PN 1622826-8 -> RC1005J123CS; PSK_PN 1622826-8 -> RC1005J123CS
- R45: MIFARE_PN RMCF0402JT2K20 -> RC1005J222CS
- R48, R49, R55, R62: ASK_PN RMCF0402JT2K20 -> RC1005J222CS; FSK_PN RMCF0402JT2K20 -> RC1005J222CS; MIFARE_PN RMCF0402JT2K20 -> RC1005J222CS; PSK_PN RMCF0402JT2K20 -> RC1005J222CS
- R6: ASK_PN RMCF0402JT2K20 -> RC1005J222CS; FSK_PN RMCF0402JT2K20 -> RC1005J222CS; PSK_CUSTOMERPN RMCF0402JT2K20 -> R/2.2k/5%/04; PSK_PN R/2.2k/5%/04 -> RC1005J222CS
